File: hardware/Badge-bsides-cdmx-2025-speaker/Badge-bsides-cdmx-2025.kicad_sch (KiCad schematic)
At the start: 42 parts, among them J1 SWDIO, J3 ADDON, J4 Conn_01x04_Pin, J5 I2C, J6 Conn_01x04_Pin, P6 USB_C_Plug_USB2.0, Q3 DMG3415U-7, SW10 SW_Push, SW11 ON, SW2 RESET, SW7 SW_Push, SW8 SW_Push, SW9 SW_Push, U1 PY32F030F28U6TR, U6 AP2112K-3.3

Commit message: feat(Hw):Update_BOM_And_Route
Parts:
- removed D10, D9: R_LED, Footprints:LYT77K-K2M1, symbol Device:LED
- removed R11, R9: 220, Resistor_SMD:R_0603_1608Metric, symbol Device:R_Small
- added C29, C30: 100nF, Capacitor_SMD:C_0603_1608Metric, symbol Device:C_Small
- added D19, D20: WS2812B, Footprints:LED_SK6812-E, symbol LED:WS2812B
- added R3: 1K, Resistor_SMD:R_0603_1608Metric, symbol Device:R
- BT3, BT4: Manufacturer_Part_Number (none) -> BH-AAA-A1AJ001
- C10, C26, C28: LCSC# C85713 -> C96446
- C6: LCSC# C66501 -> C14663
- C67, C68, C69, C70: #LCSC C96446 -> (none); LCSC# (none) -> C96446
- D4: Manufacturer_Part_Number (none) -> MBR120LSF
- F3: Manufacturer_Part_Number (none) -> 06D0750D
- J4: LCSC# (none) -> C492412
- J5: Manufacturer_Part_Number (none) -> Display OLED 128×32 0.91 I2C SSD1306 Blanco / Azul
- J6: LCSC# (none) -> C2897386
- R41, R45: Manufacturer_Part_Number (none) -> ERJ3RBD5101V
- SW10, SW7, SW8, SW9: #LCSC C455280 -> (none); LCSC# (none) -> C455280
- U6: Manufacturer_Part_Number (none) -> AP7365-33WG-7
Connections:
- net +3V3 is gone; now on net +3.3V: C26.1, J3.1 (Pin_1), R4.2, R5.2, R6.2, R7.2, R8.2, U6.5 (VOUT)
- net +3.3V: now also C29.1, C30.1, D19.1 (VDD), D20.1 (VDD)
- net GND: now also C29.2, C30.2, D19.3 (VSS), D20.3 (VSS)
- net GPIO1: now also U1.11 (PB7); no longer U1.3 (PA7)
- net GPIO2: now also U1.12 (PF4/BOOT0); no longer U1.5 (PA12)
- net RX: now also J6.3 (Pin_3), J6.4 (Pin_4); no longer J4.3 (Pin_3), J4.4 (Pin_4)
- net TX: now also J4.3 (Pin_3), J4.4 (Pin_4); no longer J6.3 (Pin_3), J6.4 (Pin_4)
- net LED1: no longer names the net of U1.10 (PB6)
- net LED2: no longer names the net of U1.20 (PA4)
- new net: D19.4 (DIN), R3.2
- new net: D19.2 (DOUT), D20.4 (DIN)
- new net NEO: R3.1, U1.3 (PA7)
- no-connect marks 3 -> 7
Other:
- title: Bsides cDMX 2025 -> Bsides CDMX Speaker 2025
- moved on the sheet: C10, C26, C6, D4, Q3, R10, R4, SW11, SW2, U6

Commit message: feat(Hw):Update_Route
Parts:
- removed C10, C26, C27: 10uF, Capacitor_SMD:C_0603_1608Metric, symbol Device:C_Small
- removed C33: 100nF, Capacitor_SMD:C_0603_1608Metric, symbol Device:C
- removed D4: MBR120, Diode_SMD:D_SOD-123F, symbol Diode:MBR340
- removed F3: 750mA, Fuse:Fuse_0603_1608Metric, symbol Device:Fuse_Small
- removed P6: USB_C_Plug_USB2.0, Footprints:C393939, symbol HunterCat-NFC-rescue:USB_C_Plug_USB2.0-Connector
- removed Q3: DMG3415U-7, Package_TO_SOT_SMD:SOT-23, symbol Device:Q_PMOS_GSD
- removed R10: 100K, Resistor_SMD:R_0603_1608Metric, symbol Device:R_Small
- removed R41, R45: 5k1, Resistor_SMD:R_0603_1608Metric, symbol Device:R_Small
- removed U6: AP2112K-3.3, Package_TO_SOT_SMD:SOT-23-5, symbol HunterCat-NFC-rescue:AP2112K-3.3-Regulator_Linear
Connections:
- net VBUS is gone; now on net +3.3V: J1.1 (Pin_1)
- net +3.3V: now also SW11.3 (A)
- net +BATT: now also SW11.2 (B)
- no-connect marks 7 -> 5
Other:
- note removed: "PSU"
- moved on the sheet: SW11

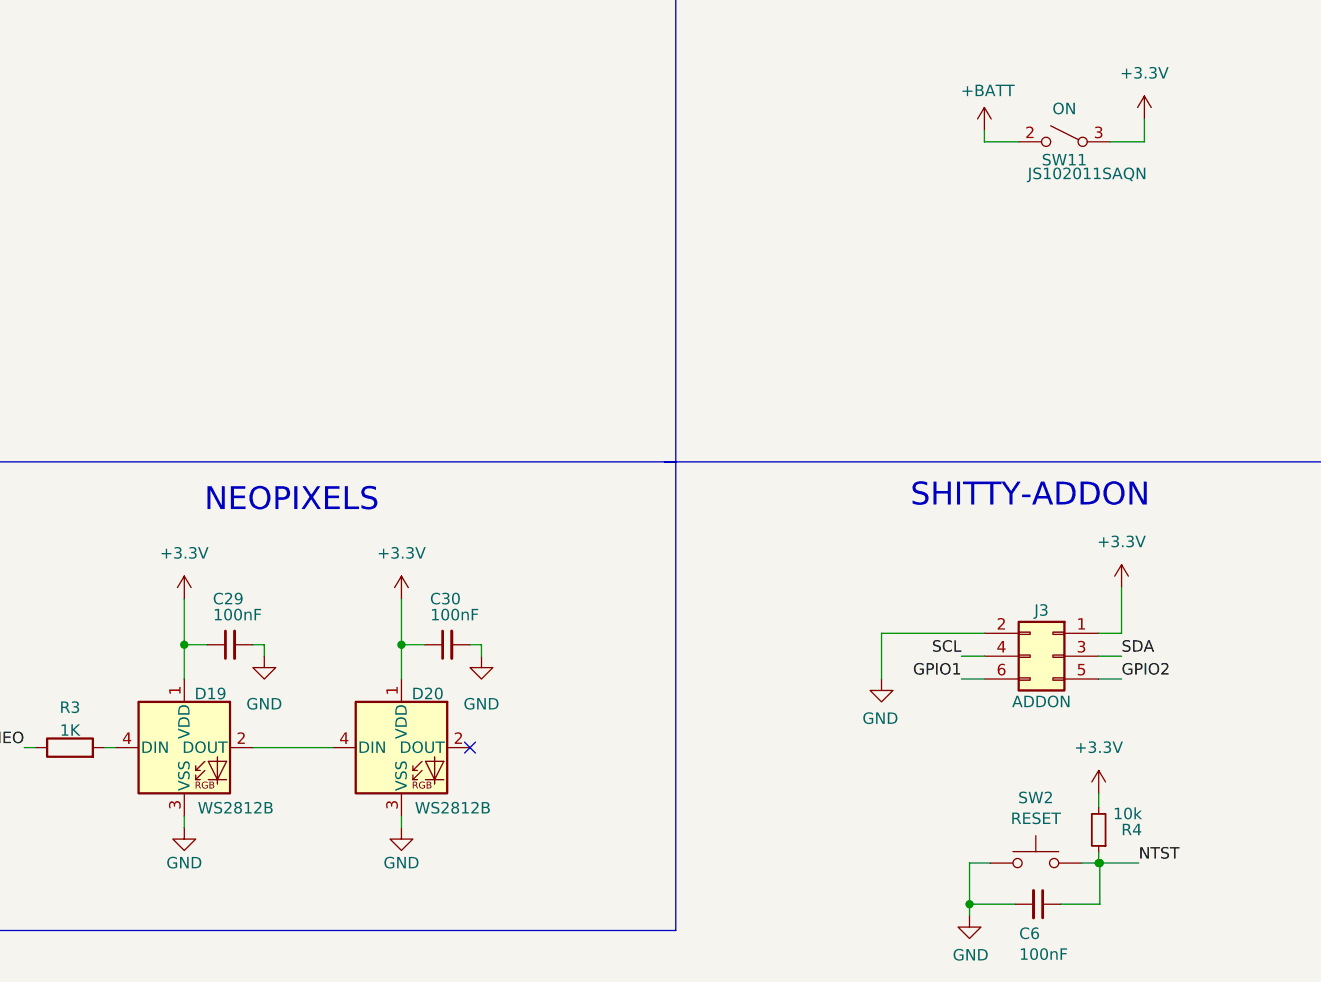
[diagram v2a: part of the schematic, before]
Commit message: Fix(Hw): Fixed_BOM(Staff,Community, Speaker)
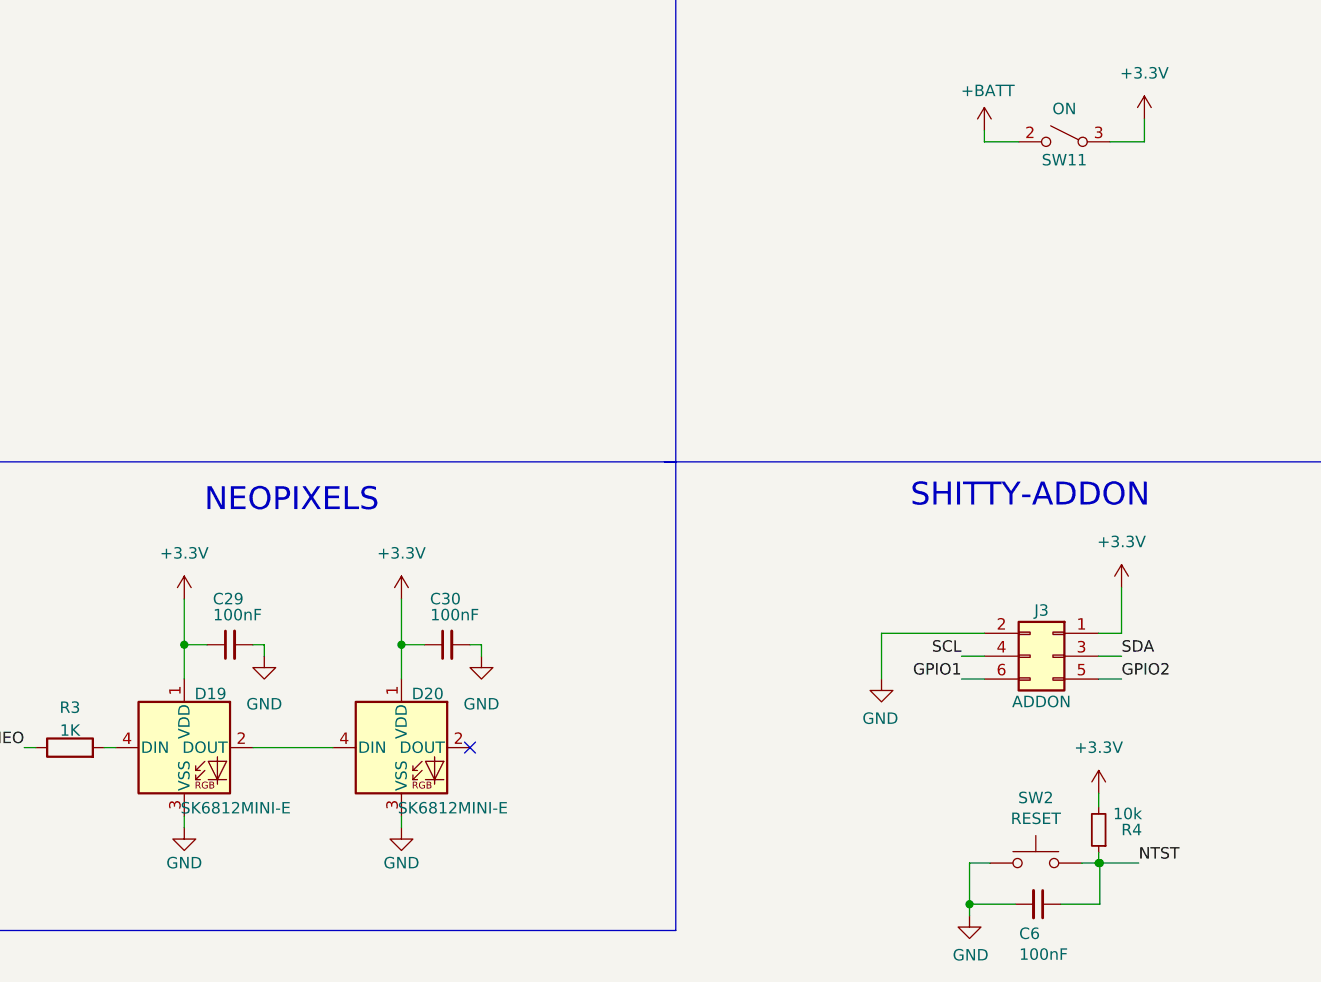
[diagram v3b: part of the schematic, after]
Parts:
- C29, C30: LCSC# C478888 -> C66501
- C34, C6: LCSC# C14663 -> C66501
- D19, D20: value WS2812B -> SK6812MINI-E; LCSC# C527089 -> C5149201; Manufacturer_Part_Number WS2812B-Mini -> (none)
- SW11: LCSC# - -> C221660; Manufacturer_Part_Number JS102011SAQN -> (none)
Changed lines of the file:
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@@
 			)
 		)
-		(property "LCSC#" "-"
+		(property "LCSC#" "C221660"
 			(at 139.7 45.72 0)
 			(effects
@@
 			)
 		)
-		(property "Manufacturer_Part_Number" "JS102011SAQN"
+		(property "Manufacturer_Part_Number" ""
 			(at 142.24 49.276 0)
 			(effects
@@
 			)
 		)
-		(property "Value" "WS2812B"
+		(property "Value" "SK6812MINI-E"
 			(at 71.755 119.761 0)
 			(effects
@@
 			)
 		)
-		(property "LCSC#" "C527089"
+		(property "LCSC#" "C5149201"
 			(at 66.04 113.03 0)
 			(effects
@@
 			)
 		)
-		(property "Manufacturer_Part_Number" "WS2812B-Mini"
+		(property "Manufacturer_Part_Number" ""
 			(at 66.04 113.03 0)
 			(effects
@@
 			)
 		)
-		(property "LCSC#" "C478888"
+		(property "LCSC#" "C66501"
 			(at 71.12 101.6 0)
 			(effects
@@
 			)
 		)
-		(property "LCSC#" "C478888"
+		(property "LCSC#" "C66501"
 			(at 46.99 101.6 0)
 			(effects
@@
 			)
 		)
-		(property "LCSC#" "C14663"
+		(property "LCSC#" "C66501"
 			(at 136.779 130.429 0)
 			(effects
@@
 			)
 		)
-		(property "LCSC#" "C14663"
+		(property "LCSC#" "C66501"
 			(at 209.296 30.48 0)
 			(effects
@@
 			)
 		)
-		(property "Value" "WS2812B"
+		(property "Value" "SK6812MINI-E"
 			(at 47.625 119.761 0)
 			(effects
@@
 			)
 		)
-		(property "LCSC#" "C527089"
+		(property "LCSC#" "C5149201"
 			(at 41.91 113.03 0)
 			(effects
@@
 			)
 		)
-		(property "Manufacturer_Part_Number" "WS2812B-Mini"
+		(property "Manufacturer_Part_Number" ""
 			(at 41.91 113.03 0)
 			(effects

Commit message: fix(Hw):Labels_Updated
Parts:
- R3: value 1K -> 470R; LCSC# C22548 -> C114669
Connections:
- net GND: now also U1.21 (VSS)
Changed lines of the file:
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@@
 			)
 		)
-		(property "Value" "1K"
+		(property "Value" "470R"
 			(at 29.21 111.125 90)
 			(effects
@@
 			)
 		)
-		(property "LCSC#" "C22548"
+		(property "LCSC#" "C114669"
 			(at 29.21 113.03 0)
 			(effects
@@
 		(pin "12"
 		)
+		(pin "21"
+		)
 		(instances
